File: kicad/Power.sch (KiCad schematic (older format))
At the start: 11 parts, among them U3 LXDC2UR30

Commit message: コンデンサを追加
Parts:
- added C5: 47u, Capacitors_SMD:C_0805, symbol Device:C
- renumbered C5 to C6
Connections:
- net +3V3: now also C5.1
- net GND: now also C5.2
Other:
- moved on the sheet: C6, D1, D2, L3, R4, R5
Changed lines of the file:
@@
 L Device:R R4
 U 1 1 57D00960
-P 5800 4450
-F 0 "R4" V 5880 4450 50  0000 C CNN
-F 1 "1k" V 5800 4450 50  0000 C CNN
-F 2 "Resistors_SMD:R_0201_NoSilk" V 5730 4450 50  0001 C CNN
-F 3 "" H 5800 4450 50  0000 C CNN
-	1    5800 4450
-	1    0    0    -1
-$EndComp
-$Comp
-L power:GND #PWR027
+P 6300 4450
+F 0 "R4" V 6380 4450 50  0000 C CNN
+F 1 "1k" V 6300 4450 50  0000 C CNN
+F 2 "Resistors_SMD:R_0201_NoSilk" V 6230 4450 50  0001 C CNN
+F 3 "" H 6300 4450 50  0000 C CNN
+	1    6300 4450
+	1    0    0    -1
+$EndComp
+$Comp
+L power:GND #PWR029
 U 1 1 57D00A42
-P 5800 5200
-F 0 "#PWR027" H 5800 4950 50  0001 C CNN
-F 1 "GND" H 5800 5050 50  0000 C CNN
-F 2 "" H 5800 5200 50  0000 C CNN
-F 3 "" H 5800 5200 50  0000 C CNN
-	1    5800 5200
+P 6300 5200
+F 0 "#PWR029" H 6300 4950 50  0001 C CNN
+F 1 "GND" H 6300 5050 50  0000 C CNN
+F 2 "" H 6300 5200 50  0000 C CNN
+F 3 "" H 6300 5200 50  0000 C CNN
+	1    6300 5200
 	1    0    0    -1
 $EndComp
@@
 $EndComp
 $Comp
-L power:+3.3V #PWR026
+L power:+3.3V #PWR028
 U 1 1 589CB64F
-P 5800 4200
-F 0 "#PWR026" H 5800 4050 50  0001 C CNN
-F 1 "+3.3V" H 5800 4340 50  0000 C CNN
-F 2 "" H 5800 4200 50  0000 C CNN
-F 3 "" H 5800 4200 50  0000 C CNN
-	1    5800 4200
+P 6300 4200
+F 0 "#PWR028" H 6300 4050 50  0001 C CNN
+F 1 "+3.3V" H 6300 4340 50  0000 C CNN
+F 2 "" H 6300 4200 50  0000 C CNN
+F 3 "" H 6300 4200 50  0000 C CNN
+	1    6300 4200
 	1    0    0    -1
 $EndComp
@@
 	2600 4200 2600 4300
 Wire Wire Line
-	5800 4700 5800 4600
-Wire Wire Line
-	5800 4300 5800 4200
+	6300 4700 6300 4600
+Wire Wire Line
+	6300 4300 6300 4200
 Wire Wire Line
 	4200 4500 4100 4500
@@
 L Device:LED D1
 U 1 1 594AB638
-P 5800 4850
-F 0 "D1" H 5800 4950 50  0000 C CNN
-F 1 "Power" H 5800 4750 50  0000 C CNN
-F 2 "LEDs:LED_0402" H 5800 4850 50  0001 C CNN
-F 3 "" H 5800 4850 50  0001 C CNN
-	1    5800 4850
+P 6300 4850
+F 0 "D1" H 6300 4950 50  0000 C CNN
+F 1 "Power" H 6300 4750 50  0000 C CNN
+F 2 "LEDs:LED_0402" H 6300 4850 50  0001 C CNN
+F 3 "" H 6300 4850 50  0001 C CNN
+	1    6300 4850
 	0    -1   -1   0
 $EndComp
 Wire Wire Line
-	5800 5000 5800 5200
-$Comp
-L power:+3.3V #PWR030
+	6300 5000 6300 5200
+$Comp
+L power:+3.3V #PWR032
 U 1 1 59C37023
-P 6600 4200
-F 0 "#PWR030" H 6600 4050 50  0001 C CNN
-F 1 "+3.3V" H 6600 4340 50  0000 C CNN
-F 2 "" H 6600 4200 50  0001 C CNN
-F 3 "" H 6600 4200 50  0001 C CNN
-	1    6600 4200
+P 7100 4200
+F 0 "#PWR032" H 7100 4050 50  0001 C CNN
+F 1 "+3.3V" H 7100 4340 50  0000 C CNN
+F 2 "" H 7100 4200 50  0001 C CNN
+F 3 "" H 7100 4200 50  0001 C CNN
+	1    7100 4200
 	1    0    0    -1
 $EndComp
@@
 L Device:L_Small L3
 U 1 1 59C3706B
-P 6800 4300
-F 0 "L3" H 6830 4340 50  0000 L CNN
-F 1 "100u" H 6830 4260 50  0000 L CNN
-F 2 "Capacitors_SMD:C_0603" H 6800 4300 50  0001 C CNN
-F 3 "" H 6800 4300 50  0001 C CNN
-	1    6800 4300
+P 7300 4300
+F 0 "L3" H 7330 4340 50  0000 L CNN
+F 1 "100u" H 7330 4260 50  0000 L CNN
+F 2 "Capacitors_SMD:C_0603" H 7300 4300 50  0001 C CNN
+F 3 "" H 7300 4300 50  0001 C CNN
+	1    7300 4300
 	0    1    1    0
 $EndComp
 $Comp
-L Device:C_Small C5
+L Device:C_Small C6
 U 1 1 59C370C1
-P 7000 4500
-F 0 "C5" H 7010 4570 50  0000 L CNN
-F 1 "10u" H 7010 4420 50  0000 L CNN
-F 2 "Capacitors_SMD:C_0402_NoSilk" H 7000 4500 50  0001 C CNN
-F 3 "" H 7000 4500 50  0001 C CNN
-	1    7000 4500
-	1    0    0    -1
-$EndComp
-Wire Wire Line
-	7000 4200 7000 4300
-$Comp
-L power:GND #PWR032
+P 7500 4500
+F 0 "C6" H 7510 4570 50  0000 L CNN
+F 1 "10u" H 7510 4420 50  0000 L CNN
+F 2 "Capacitors_SMD:C_0402_NoSilk" H 7500 4500 50  0001 C CNN
+F 3 "" H 7500 4500 50  0001 C CNN
+	1    7500 4500
+	1    0    0    -1
+$EndComp
+Wire Wire Line
+	7500 4200 7500 4300
+$Comp
+L power:GND #PWR034
 U 1 1 59C37170
-P 7000 4700
-F 0 "#PWR032" H 7000 4450 50  0001 C CNN
-F 1 "GND" H 7000 4550 50  0000 C CNN
-F 2 "" H 7000 4700 50  0000 C CNN
-F 3 "" H 7000 4700 50  0000 C CNN
-	1    7000 4700
-	1    0    0    -1
-$EndComp
-Wire Wire Line
-	7000 4700 7000 4600
-Wire Wire Line
-	6900 4300 7000 4300
-Connection ~ 7000 4300
-Wire Wire Line
-	6700 4300 6600 4300
-Wire Wire Line
-	6600 4300 6600 4200
+P 7500 4700
+F 0 "#PWR034" H 7500 4450 50  0001 C CNN
+F 1 "GND" H 7500 4550 50  0000 C CNN
+F 2 "" H 7500 4700 50  0000 C CNN
+F 3 "" H 7500 4700 50  0000 C CNN
+	1    7500 4700
+	1    0    0    -1
+$EndComp
+Wire Wire Line
+	7500 4700 7500 4600
+Wire Wire Line
+	7400 4300 7500 4300
+Connection ~ 7500 4300
+Wire Wire Line
+	7200 4300 7100 4300
+Wire Wire Line
+	7100 4300 7100 4200
 $Comp
 L Device:C_Small C4
@@
 L power:PWR_FLAG #FLG03
 U 1 1 5A1BE075
-P 7200 4300
-F 0 "#FLG03" H 7200 4375 50  0001 C CNN
-F 1 "PWR_FLAG" H 7200 4450 50  0000 C CNN
-F 2 "" H 7200 4300 50  0001 C CNN
-F 3 "" H 7200 4300 50  0001 C CNN
-	1    7200 4300
+P 7700 4300
+F 0 "#FLG03" H 7700 4375 50  0001 C CNN
+F 1 "PWR_FLAG" H 7700 4450 50  0000 C CNN
+F 2 "" H 7700 4300 50  0001 C CNN
+F 3 "" H 7700 4300 50  0001 C CNN
+	1    7700 4300
 	0    1    1    0
 $EndComp
@@
 L Device:R R5
 U 1 1 5A4BB521
-P 6100 4450
-F 0 "R5" V 6180 4450 50  0000 C CNN
-F 1 "1k" V 6100 4450 50  0000 C CNN
-F 2 "Resistors_SMD:R_0201_NoSilk" V 6030 4450 50  0001 C CNN
-F 3 "" H 6100 4450 50  0000 C CNN
-	1    6100 4450
-	1    0    0    -1
-$EndComp
-$Comp
-L power:GND #PWR029
+P 6600 4450
+F 0 "R5" V 6680 4450 50  0000 C CNN
+F 1 "1k" V 6600 4450 50  0000 C CNN
+F 2 "Resistors_SMD:R_0201_NoSilk" V 6530 4450 50  0001 C CNN
+F 3 "" H 6600 4450 50  0000 C CNN
+	1    6600 4450
+	1    0    0    -1
+$EndComp
+$Comp
+L power:GND #PWR031
 U 1 1 5A4BB527
-P 6100 5200
-F 0 "#PWR029" H 6100 4950 50  0001 C CNN
-F 1 "GND" H 6100 5050 50  0000 C CNN
-F 2 "" H 6100 5200 50  0000 C CNN
-F 3 "" H 6100 5200 50  0000 C CNN
-	1    6100 5200
-	1    0    0    -1
-$EndComp
-$Comp
-L power:+3.3V #PWR028
+P 6600 5200
+F 0 "#PWR031" H 6600 4950 50  0001 C CNN
+F 1 "GND" H 6600 5050 50  0000 C CNN
+F 2 "" H 6600 5200 50  0000 C CNN
+F 3 "" H 6600 5200 50  0000 C CNN
+	1    6600 5200
+	1    0    0    -1
+$EndComp
+$Comp
+L power:+3.3V #PWR030
 U 1 1 5A4BB52D
-P 6100 4200
-F 0 "#PWR028" H 6100 4050 50  0001 C CNN
-F 1 "+3.3V" H 6100 4340 50  0000 C CNN
-F 2 "" H 6100 4200 50  0000 C CNN
-F 3 "" H 6100 4200 50  0000 C CNN
-	1    6100 4200
-	1    0    0    -1
-$EndComp
-Wire Wire Line
-	6100 4700 6100 4600
-Wire Wire Line
-	6100 4300 6100 4200
+P 6600 4200
+F 0 "#PWR030" H 6600 4050 50  0001 C CNN
+F 1 "+3.3V" H 6600 4340 50  0000 C CNN
+F 2 "" H 6600 4200 50  0000 C CNN
+F 3 "" H 6600 4200 50  0000 C CNN
+	1    6600 4200
+	1    0    0    -1
+$EndComp
+Wire Wire Line
+	6600 4700 6600 4600
+Wire Wire Line
+	6600 4300 6600 4200
 $Comp
 L Device:LED D2
 U 1 1 5A4BB535
-P 6100 4850
-F 0 "D2" H 6100 4950 50  0000 C CNN
-F 1 "Power" H 6100 4750 50  0000 C CNN
-F 2 "LEDs:LED_0402" H 6100 4850 50  0001 C CNN
-F 3 "" H 6100 4850 50  0001 C CNN
-	1    6100 4850
+P 6600 4850
+F 0 "D2" H 6600 4950 50  0000 C CNN
+F 1 "Power" H 6600 4750 50  0000 C CNN
+F 2 "LEDs:LED_0402" H 6600 4850 50  0001 C CNN
+F 3 "" H 6600 4850 50  0001 C CNN
+	1    6600 4850
 	0    -1   -1   0
 $EndComp
 Wire Wire Line
-	6100 5000 6100 5200
+	6600 5000 6600 5200
 Wire Wire Line
 	5300 4400 5200 4400
@@
 	5300 4400 5300 4500
 Wire Wire Line
-	7000 4300 7000 4400
-Wire Wire Line
-	7000 4300 7200 4300
+	7500 4300 7500 4400
+Wire Wire Line
+	7500 4300 7700 4300
 Wire Wire Line
 	3300 4700 3400 4700
@@
 	2000 4500 2000 4200
 $Comp
-L power:VDDA #PWR031
+L power:VDDA #PWR033
 U 1 1 59C37047
-P 7000 4200
-F 0 "#PWR031" H 7000 4050 50  0001 C CNN
-F 1 "VDDA" H 7000 4350 50  0000 C CNN
-F 2 "" H 7000 4200 50  0001 C CNN
-F 3 "" H 7000 4200 50  0001 C CNN
-	1    7000 4200
+P 7500 4200
+F 0 "#PWR033" H 7500 4050 50  0001 C CNN
+F 1 "VDDA" H 7500 4350 50  0000 C CNN
+F 2 "" H 7500 4200 50  0001 C CNN
+F 3 "" H 7500 4200 50  0001 C CNN
+	1    7500 4200
 	1    0    0    -1
 $EndComp
@@
 	1    0    0    -1
 $EndComp
+$Comp
+L Device:C C5
+U 1 1 5B93EBC5
+P 5700 4750
+F 0 "C5" H 5815 4796 50  0000 L CNN
+F 1 "47u" H 5815 4705 50  0000 L CNN
+F 2 "Capacitors_SMD:C_0805" H 5738 4600 50  0001 C CNN
+F 3 "~" H 5700 4750 50  0001 C CNN
+	1    5700 4750
+	1    0    0    -1
+$EndComp
+$Comp
+L power:GND #PWR027
+U 1 1 5B93EC2F
+P 5700 5200
+F 0 "#PWR027" H 5700 4950 50  0001 C CNN
+F 1 "GND" H 5700 5050 50  0000 C CNN
+F 2 "" H 5700 5200 50  0000 C CNN
+F 3 "" H 5700 5200 50  0000 C CNN
+	1    5700 5200
+	1    0    0    -1
+$EndComp
+Wire Wire Line
+	5700 4900 5700 5200
+$Comp
+L power:+3.3V #PWR026
+U 1 1 5B93F57B
+P 5700 4200
+F 0 "#PWR026" H 5700 4050 50  0001 C CNN
+F 1 "+3.3V" H 5700 4340 50  0000 C CNN
+F 2 "" H 5700 4200 50  0000 C CNN
+F 3 "" H 5700 4200 50  0000 C CNN
+	1    5700 4200
+	1    0    0    -1
+$EndComp
+Wire Wire Line
+	5700 4200 5700 4600
 $EndSCHEMATC

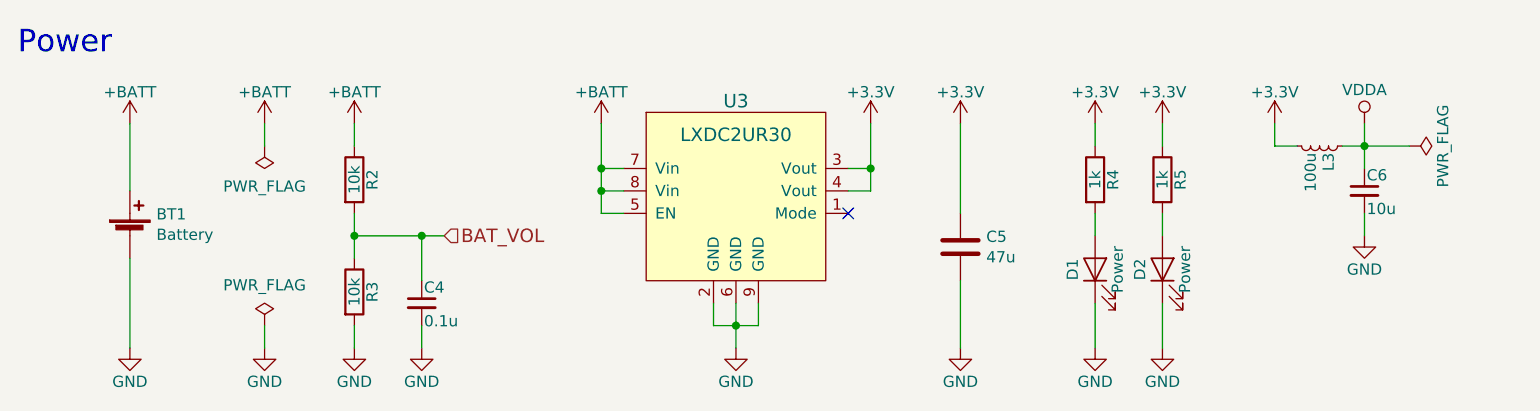
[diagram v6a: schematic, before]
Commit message: KERISEv4-5に向けて回路図を更新
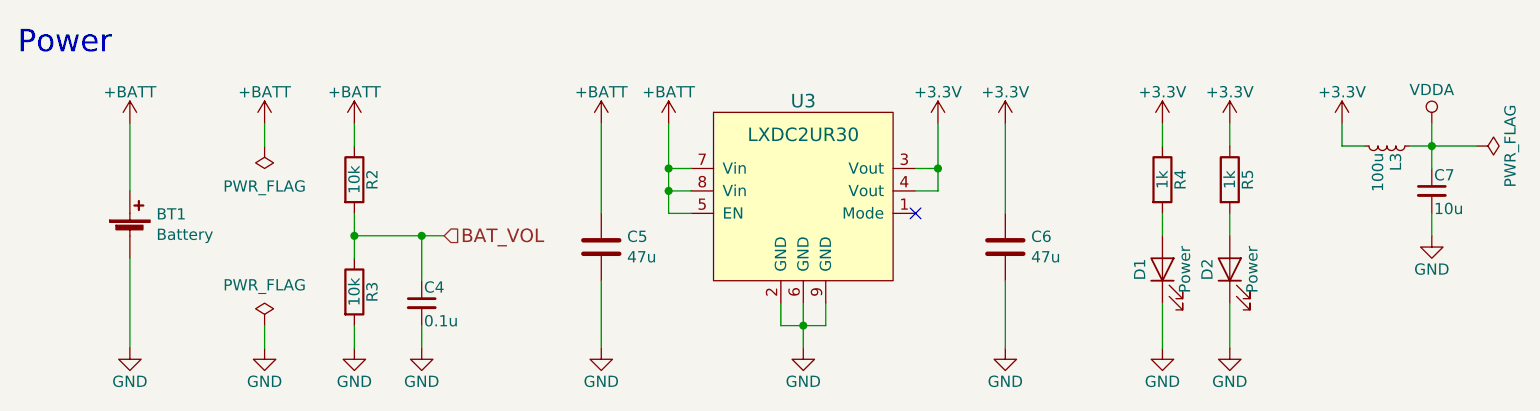
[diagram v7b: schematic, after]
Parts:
- added C5: 47u, Capacitors_SMD:C_0805, symbol Device:C
- renumbered C5 to C6, C6 to C7
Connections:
- net +BATT: now also C5.1
- net GND: now also C5.2
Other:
- moved on the sheet: C6, C7, D1, D2, L3, R4, R5, U3

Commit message: フットプリントを割り当て
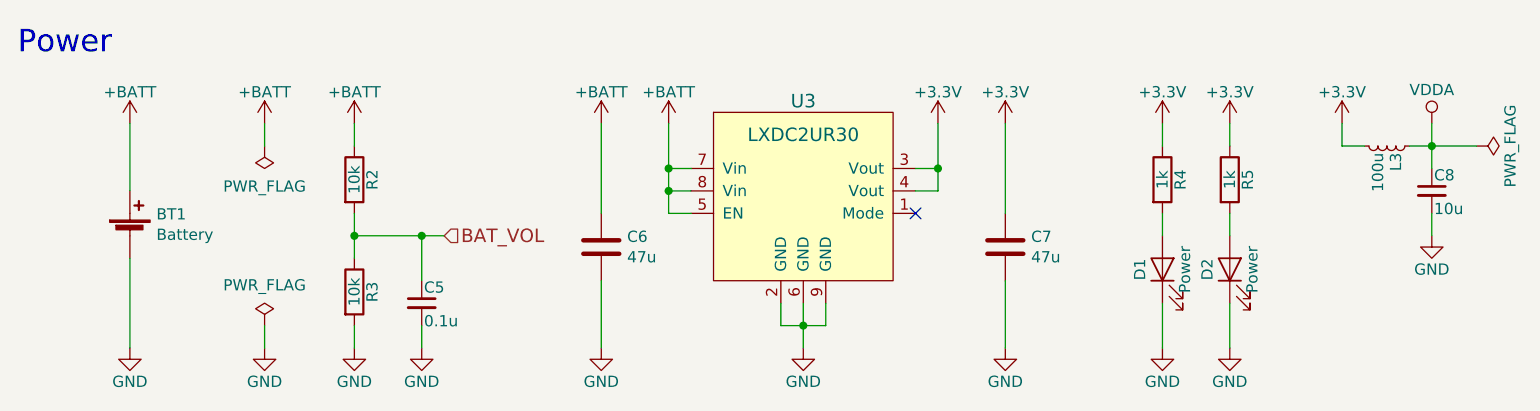
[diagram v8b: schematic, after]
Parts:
- C5: renamed from C4; footprint Capacitors_SMD:C_0201_NoSilk -> Capacitor_SMD:C_0201_0603Metric
- C6: renamed from C5; footprint Capacitors_SMD:C_0805 -> Capacitor_SMD:C_0805_2012Metric
- C7: renamed from C6; footprint Capacitors_SMD:C_0805 -> Capacitor_SMD:C_0805_2012Metric
- C8: renamed from C7; footprint Capacitors_SMD:C_0402_NoSilk -> Capacitor_SMD:C_0402_1005Metric
- D1, D2: footprint LEDs:LED_0402 -> LED_SMD:LED_0402_1005Metric
- R2, R3, R4, R5: footprint Resistors_SMD:R_0201_NoSilk -> Resistor_SMD:R_0201_0603Metric
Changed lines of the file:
@@
 $EndDescr
 $Comp
-L power:+BATT #PWR016
+L power:+BATT #PWR018
 U 1 1 57CC111A
 P 2000 4200
-F 0 "#PWR016" H 2000 4050 50  0001 C CNN
+F 0 "#PWR018" H 2000 4050 50  0001 C CNN
 F 1 "+BATT" H 2000 4340 50  0000 C CNN
 F 2 "" H 2000 4200 50  0000 C CNN
@@
 F 0 "R2" V 3080 4450 50  0000 C CNN
 F 1 "10k" V 3000 4450 50  0000 C CNN
-F 2 "Resistors_SMD:R_0201_NoSilk" V 2930 4450 50  0001 C CNN
+F 2 "Resistor_SMD:R_0201_0603Metric" V 2930 4450 50  0001 C CNN
 F 3 "" H 3000 4450 50  0000 C CNN
 	1    3000 4450
@@
 F 0 "R3" V 3080 4950 50  0000 C CNN
 F 1 "10k" V 3000 4950 50  0000 C CNN
-F 2 "Resistors_SMD:R_0201_NoSilk" V 2930 4950 50  0001 C CNN
+F 2 "Resistor_SMD:R_0201_0603Metric" V 2930 4950 50  0001 C CNN
 F 3 "" H 3000 4950 50  0000 C CNN
 	1    3000 4950
@@
 $EndComp
 $Comp
-L power:+BATT #PWR018
+L power:+BATT #PWR020
 U 1 1 57D1923B
 P 2600 4200
-F 0 "#PWR018" H 2600 4050 50  0001 C CNN
+F 0 "#PWR020" H 2600 4050 50  0001 C CNN
 F 1 "+BATT" H 2600 4340 50  0000 C CNN
 F 2 "" H 2600 4200 50  0000 C CNN
@@
 F 0 "R4" V 6680 4450 50  0000 C CNN
 F 1 "1k" V 6600 4450 50  0000 C CNN
-F 2 "Resistors_SMD:R_0201_NoSilk" V 6530 4450 50  0001 C CNN
+F 2 "Resistor_SMD:R_0201_0603Metric" V 6530 4450 50  0001 C CNN
 F 3 "" H 6600 4450 50  0000 C CNN
 	1    6600 4450
@@
 $EndComp
 $Comp
-L power:GND #PWR031
+L power:GND #PWR033
 U 1 1 57D00A42
 P 6600 5200
-F 0 "#PWR031" H 6600 4950 50  0001 C CNN
+F 0 "#PWR033" H 6600 4950 50  0001 C CNN
 F 1 "GND" H 6600 5050 50  0000 C CNN
 F 2 "" H 6600 5200 50  0000 C CNN
@@
 $EndComp
 $Comp
-L power:+BATT #PWR020
+L power:+BATT #PWR022
 U 1 1 57CD3CA2
 P 3000 4200
-F 0 "#PWR020" H 3000 4050 50  0001 C CNN
+F 0 "#PWR022" H 3000 4050 50  0001 C CNN
 F 1 "+BATT" H 3000 4340 50  0000 C CNN
 F 2 "" H 3000 4200 50  0000 C CNN
@@
 $EndComp
 $Comp
-L power:+3.3V #PWR030
+L power:+3.3V #PWR032
 U 1 1 589CB64F
 P 6600 4200
-F 0 "#PWR030" H 6600 4050 50  0001 C CNN
+F 0 "#PWR032" H 6600 4050 50  0001 C CNN
 F 1 "+3.3V" H 6600 4340 50  0000 C CNN
 F 2 "" H 6600 4200 50  0000 C CNN
@@
 $EndComp
 $Comp
-L power:+BATT #PWR025
+L power:+BATT #PWR027
 U 1 1 592A5000
 P 4400 4200
-F 0 "#PWR025" H 4400 4050 50  0001 C CNN
+F 0 "#PWR027" H 4400 4050 50  0001 C CNN
 F 1 "+BATT" H 4400 4340 50  0000 C CNN
 F 2 "" H 4400 4200 50  0000 C CNN
@@
 F 0 "D1" H 6600 4950 50  0000 C CNN
 F 1 "Power" H 6600 4750 50  0000 C CNN
-F 2 "LEDs:LED_0402" H 6600 4850 50  0001 C CNN
+F 2 "LED_SMD:LED_0402_1005Metric" H 6600 4850 50  0001 C CNN
 F 3 "" H 6600 4850 50  0001 C CNN
 	1    6600 4850
@@
 	6600 5000 6600 5200
 $Comp
-L power:+3.3V #PWR034
+L power:+3.3V #PWR036
 U 1 1 59C37023
 P 7400 4200
-F 0 "#PWR034" H 7400 4050 50  0001 C CNN
+F 0 "#PWR036" H 7400 4050 50  0001 C CNN
 F 1 "+3.3V" H 7400 4340 50  0000 C CNN
 F 2 "" H 7400 4200 50  0001 C CNN
@@
 $EndComp
 $Comp
-L Device:C_Small C7
+L Device:C_Small C8
 U 1 1 59C370C1
 P 7800 4500
-F 0 "C7" H 7810 4570 50  0000 L CNN
+F 0 "C8" H 7810 4570 50  0000 L CNN
 F 1 "10u" H 7810 4420 50  0000 L CNN
-F 2 "Capacitors_SMD:C_0402_NoSilk" H 7800 4500 50  0001 C CNN
+F 2 "Capacitor_SMD:C_0402_1005Metric" H 7800 4500 50  0001 C CNN
 F 3 "" H 7800 4500 50  0001 C CNN
 	1    7800 4500
@@
 	7800 4200 7800 4300
 $Comp
-L power:GND #PWR036
+L power:GND #PWR038
 U 1 1 59C37170
 P 7800 4700
-F 0 "#PWR036" H 7800 4450 50  0001 C CNN
+F 0 "#PWR038" H 7800 4450 50  0001 C CNN
 F 1 "GND" H 7800 4550 50  0000 C CNN
 F 2 "" H 7800 4700 50  0000 C CNN
@@
 	7400 4300 7400 4200
 $Comp
-L Device:C_Small C4
+L Device:C_Small C5
 U 1 1 59C47577
 P 3300 5000
-F 0 "C4" H 3310 5070 50  0000 L CNN
+F 0 "C5" H 3310 5070 50  0000 L CNN
 F 1 "0.1u" H 3310 4920 50  0000 L CNN
-F 2 "Capacitors_SMD:C_0201_NoSilk" H 3300 5000 50  0001 C CNN
+F 2 "Capacitor_SMD:C_0201_0603Metric" H 3300 5000 50  0001 C CNN
 F 3 "" H 3300 5000 50  0001 C CNN
 	1    3300 5000
@@
 F 0 "R5" V 6980 4450 50  0000 C CNN
 F 1 "1k" V 6900 4450 50  0000 C CNN
-F 2 "Resistors_SMD:R_0201_NoSilk" V 6830 4450 50  0001 C CNN
+F 2 "Resistor_SMD:R_0201_0603Metric" V 6830 4450 50  0001 C CNN
 F 3 "" H 6900 4450 50  0000 C CNN
 	1    6900 4450
@@
 $EndComp
 $Comp
-L power:GND #PWR033
+L power:GND #PWR035
 U 1 1 5A4BB527
 P 6900 5200
-F 0 "#PWR033" H 6900 4950 50  0001 C CNN
+F 0 "#PWR035" H 6900 4950 50  0001 C CNN
 F 1 "GND" H 6900 5050 50  0000 C CNN
 F 2 "" H 6900 5200 50  0000 C CNN
@@
 $EndComp
 $Comp
-L power:+3.3V #PWR032
+L power:+3.3V #PWR034
 U 1 1 5A4BB52D
 P 6900 4200
-F 0 "#PWR032" H 6900 4050 50  0001 C CNN
+F 0 "#PWR034" H 6900 4050 50  0001 C CNN
 F 1 "+3.3V" H 6900 4340 50  0000 C CNN
 F 2 "" H 6900 4200 50  0000 C CNN
@@
 F 0 "D2" H 6900 4950 50  0000 C CNN
 F 1 "Power" H 6900 4750 50  0000 C CNN
-F 2 "LEDs:LED_0402" H 6900 4850 50  0001 C CNN
+F 2 "LED_SMD:LED_0402_1005Metric" H 6900 4850 50  0001 C CNN
 F 3 "" H 6900 4850 50  0001 C CNN
 	1    6900 4850
@@
 	2000 4500 2000 4200
 $Comp
-L power:VDDA #PWR035
+L power:VDDA #PWR037
 U 1 1 59C37047
 P 7800 4200
-F 0 "#PWR035" H 7800 4050 50  0001 C CNN
+F 0 "#PWR037" H 7800 4050 50  0001 C CNN
 F 1 "VDDA" H 7800 4350 50  0000 C CNN
 F 2 "" H 7800 4200 50  0001 C CNN
@@
 	3000 4700 3000 4800
 $Comp
-L power:GND #PWR021
+L power:GND #PWR023
 U 1 1 5B6FEDB1
 P 3000 5200
-F 0 "#PWR021" H 3000 4950 50  0001 C CNN
+F 0 "#PWR023" H 3000 4950 50  0001 C CNN
 F 1 "GND" H 3000 5050 50  0000 C CNN
 F 2 "" H 3000 5200 50  0000 C CNN
@@
 $EndComp
 $Comp
-L power:GND #PWR022
+L power:GND #PWR024
 U 1 1 5B6FEDD6
 P 3300 5200
-F 0 "#PWR022" H 3300 4950 50  0001 C CNN
+F 0 "#PWR024" H 3300 4950 50  0001 C CNN
 F 1 "GND" H 3300 5050 50  0000 C CNN
 F 2 "" H 3300 5200 50  0000 C CNN
@@
 $EndComp
 $Comp
-L power:GND #PWR019
+L power:GND #PWR021
 U 1 1 5B705567
 P 2600 5200
-F 0 "#PWR019" H 2600 4950 50  0001 C CNN
+F 0 "#PWR021" H 2600 4950 50  0001 C CNN
 F 1 "GND" H 2600 5050 50  0000 C CNN
 F 2 "" H 2600 5200 50  0000 C CNN
@@
 $EndComp
 $Comp
-L power:GND #PWR026
+L power:GND #PWR028
 U 1 1 5B70558C
 P 5000 5200
-F 0 "#PWR026" H 5000 4950 50  0001 C CNN
+F 0 "#PWR028" H 5000 4950 50  0001 C CNN
 F 1 "GND" H 5000 5050 50  0000 C CNN
 F 2 "" H 5000 5200 50  0000 C CNN
@@
 $EndComp
 $Comp
-L power:+3.3V #PWR027
+L power:+3.3V #PWR029
 U 1 1 5B705DFE
 P 5600 4200
-F 0 "#PWR027" H 5600 4050 50  0001 C CNN
+F 0 "#PWR029" H 5600 4050 50  0001 C CNN
 F 1 "+3.3V" H 5600 4340 50  0000 C CNN
 F 2 "" H 5600 4200 50  0000 C CNN
@@
 $EndComp
 $Comp
-L power:GND #PWR017
+L power:GND #PWR019
 U 1 1 5B707C07
 P 2000 5200
-F 0 "#PWR017" H 2000 4950 50  0001 C CNN
+F 0 "#PWR019" H 2000 4950 50  0001 C CNN
 F 1 "GND" H 2000 5050 50  0000 C CNN
 F 2 "" H 2000 5200 50  0000 C CNN
@@
 $EndComp
 $Comp
-L Device:C C6
+L Device:C C7
 U 1 1 5B93EBC5
 P 5900 4750
-F 0 "C6" H 6015 4796 50  0000 L CNN
+F 0 "C7" H 6015 4796 50  0000 L CNN
 F 1 "47u" H 6015 4705 50  0000 L CNN
-F 2 "Capacitors_SMD:C_0805" H 5938 4600 50  0001 C CNN
+F 2 "Capacitor_SMD:C_0805_2012Metric" H 5938 4600 50  0001 C CNN
 F 3 "~" H 5900 4750 50  0001 C CNN
 	1    5900 4750
@@
 $EndComp
 $Comp
-L power:GND #PWR029
+L power:GND #PWR031
 U 1 1 5B93EC2F
 P 5900 5200
-F 0 "#PWR029" H 5900 4950 50  0001 C CNN
+F 0 "#PWR031" H 5900 4950 50  0001 C CNN
 F 1 "GND" H 5900 5050 50  0000 C CNN
 F 2 "" H 5900 5200 50  0000 C CNN
@@
 	5900 4900 5900 5200
 $Comp
-L power:+3.3V #PWR028
+L power:+3.3V #PWR030
 U 1 1 5B93F57B
 P 5900 4200
-F 0 "#PWR028" H 5900 4050 50  0001 C CNN
+F 0 "#PWR030" H 5900 4050 50  0001 C CNN
 F 1 "+3.3V" H 5900 4340 50  0000 C CNN
 F 2 "" H 5900 4200 50  0000 C CNN
@@
 	5900 4200 5900 4600
 $Comp
-L Device:C C5
+L Device:C C6
 U 1 1 5C2A0D61
 P 4100 4750
-F 0 "C5" H 4215 4796 50  0000 L CNN
+F 0 "C6" H 4215 4796 50  0000 L CNN
 F 1 "47u" H 4215 4705 50  0000 L CNN
-F 2 "Capacitors_SMD:C_0805" H 4138 4600 50  0001 C CNN
+F 2 "Capacitor_SMD:C_0805_2012Metric" H 4138 4600 50  0001 C CNN
 F 3 "~" H 4100 4750 50  0001 C CNN
 	1    4100 4750
@@
 $EndComp
 $Comp
-L power:+BATT #PWR023
+L power:+BATT #PWR025
 U 1 1 5C2A0DD3
 P 4100 4200
-F 0 "#PWR023" H 4100 4050 50  0001 C CNN
+F 0 "#PWR025" H 4100 4050 50  0001 C CNN
 F 1 "+BATT" H 4100 4340 50  0000 C CNN
 F 2 "" H 4100 4200 50  0000 C CNN
@@
 $EndComp
 $Comp
-L power:GND #PWR024
+L power:GND #PWR026
 U 1 1 5C2A0DF8
 P 4100 5200
-F 0 "#PWR024" H 4100 4950 50  0001 C CNN
+F 0 "#PWR026" H 4100 4950 50  0001 C CNN
 F 1 "GND" H 4100 5050 50  0000 C CNN
 F 2 "" H 4100 5200 50  0000 C CNN
